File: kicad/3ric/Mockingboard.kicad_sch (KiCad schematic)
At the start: 18 parts

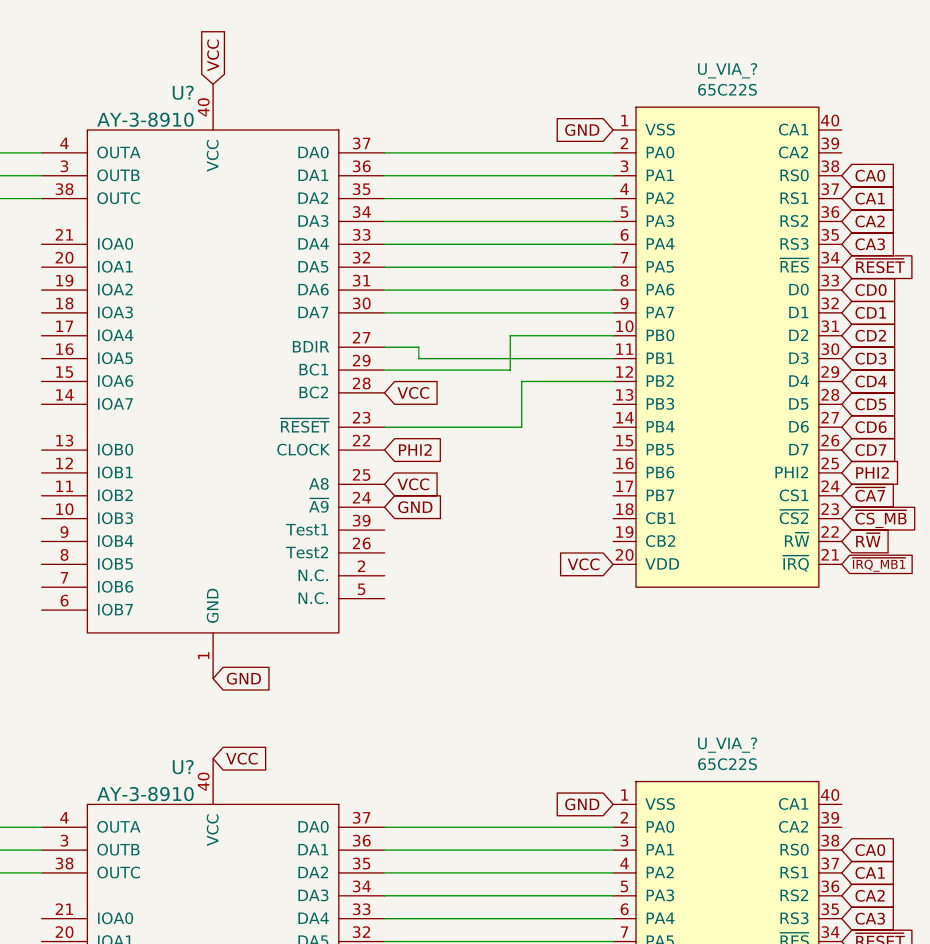
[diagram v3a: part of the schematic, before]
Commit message: update schematic based on breadboard
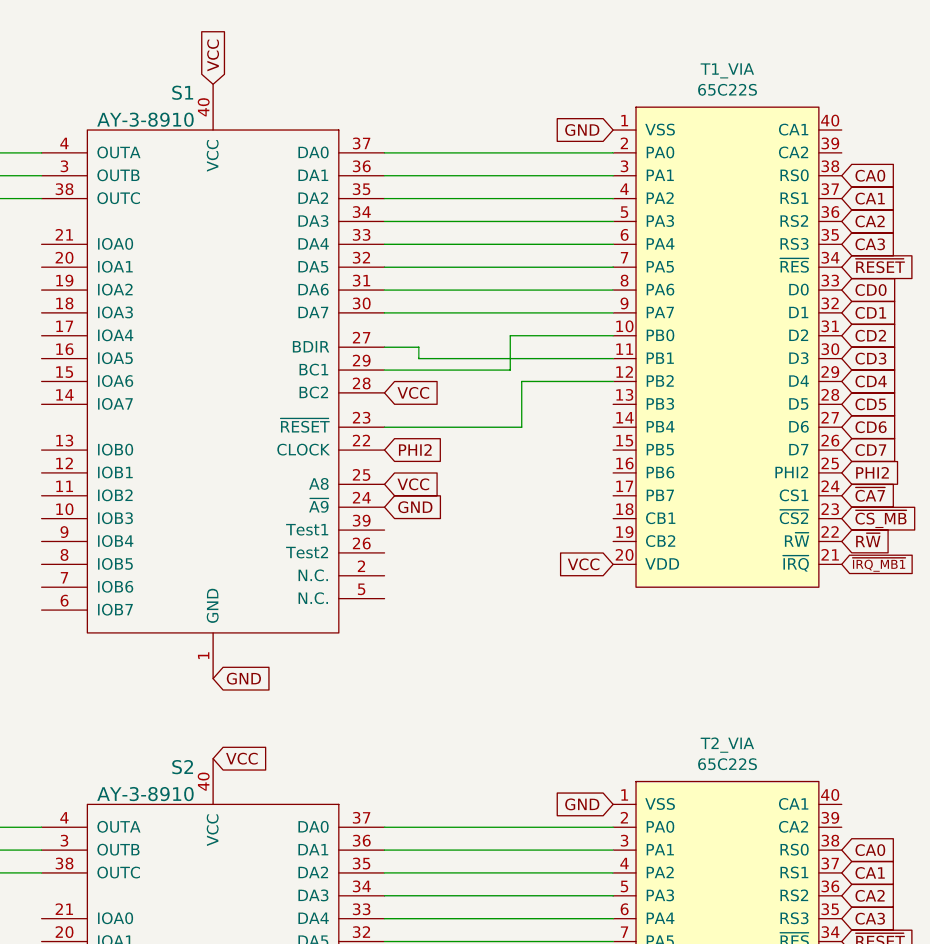
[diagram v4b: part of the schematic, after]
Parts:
- gave numbers to parts that had none: 4
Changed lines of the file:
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@@
 		(on_board yes)
 		(dnp no)
-		(property "Reference" "U_VIA_?"
+		(property "Reference" "T1_VIA"
 			(at 193.04 23.749 0)
 			(effects
@@
 			(project "3ric"
 				(path "/e63e39d7-6ac0-4ffd-8aa3-1841a4541b55/daee66e3-1acf-4bf2-888e-d1288a5b77db"
-					(reference "U_VIA_?")
+					(reference "T1_VIA")
 					(unit 1)
 				)
@@
 		(dnp no)
 		(fields_autoplaced yes)
-		(property "Reference" "U?"
+		(property "Reference" "S2"
 			(at 133.8706 101.3259 0)
 			(effects
@@
 			(project "3ric"
 				(path "/e63e39d7-6ac0-4ffd-8aa3-1841a4541b55/daee66e3-1acf-4bf2-888e-d1288a5b77db"
-					(reference "U?")
+					(reference "S2")
 					(unit 1)
 				)
@@
 		(on_board yes)
 		(dnp no)
-		(property "Reference" "U_VIA_?"
+		(property "Reference" "T2_VIA"
 			(at 193.04 98.679 0)
 			(effects
@@
 			(project "3ric"
 				(path "/e63e39d7-6ac0-4ffd-8aa3-1841a4541b55/daee66e3-1acf-4bf2-888e-d1288a5b77db"
-					(reference "U_VIA_?")
+					(reference "T2_VIA")
 					(unit 1)
 				)
@@
 		(dnp no)
 		(fields_autoplaced yes)
-		(property "Reference" "U?"
+		(property "Reference" "S1"
 			(at 133.8706 26.3959 0)
 			(effects
@@
 			(project "3ric"
 				(path "/e63e39d7-6ac0-4ffd-8aa3-1841a4541b55/daee66e3-1acf-4bf2-888e-d1288a5b77db"
-					(reference "U?")
+					(reference "S1")
 					(unit 1)
 				)

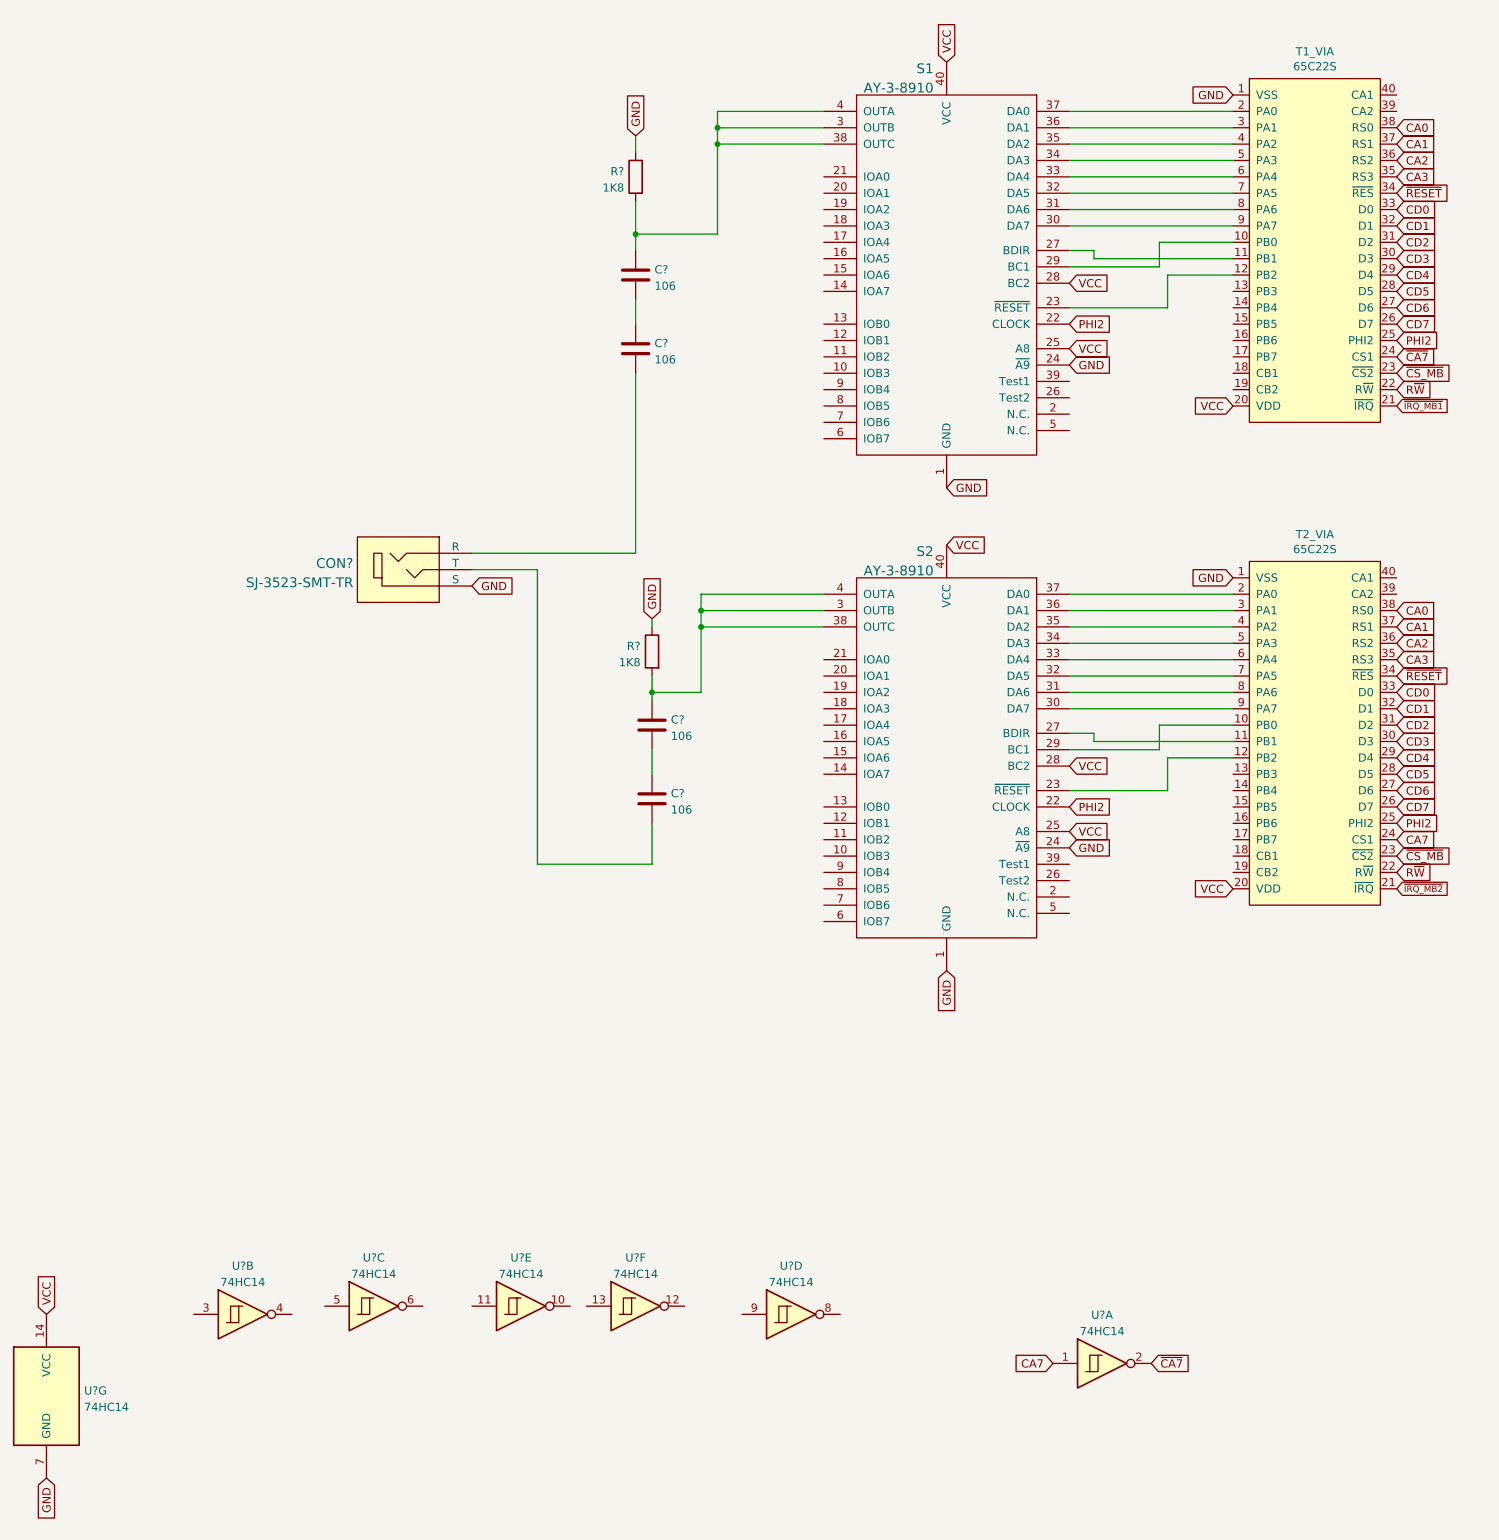
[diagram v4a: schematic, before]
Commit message: completed?  Everything wired in layout creator and first draft of completed schematic
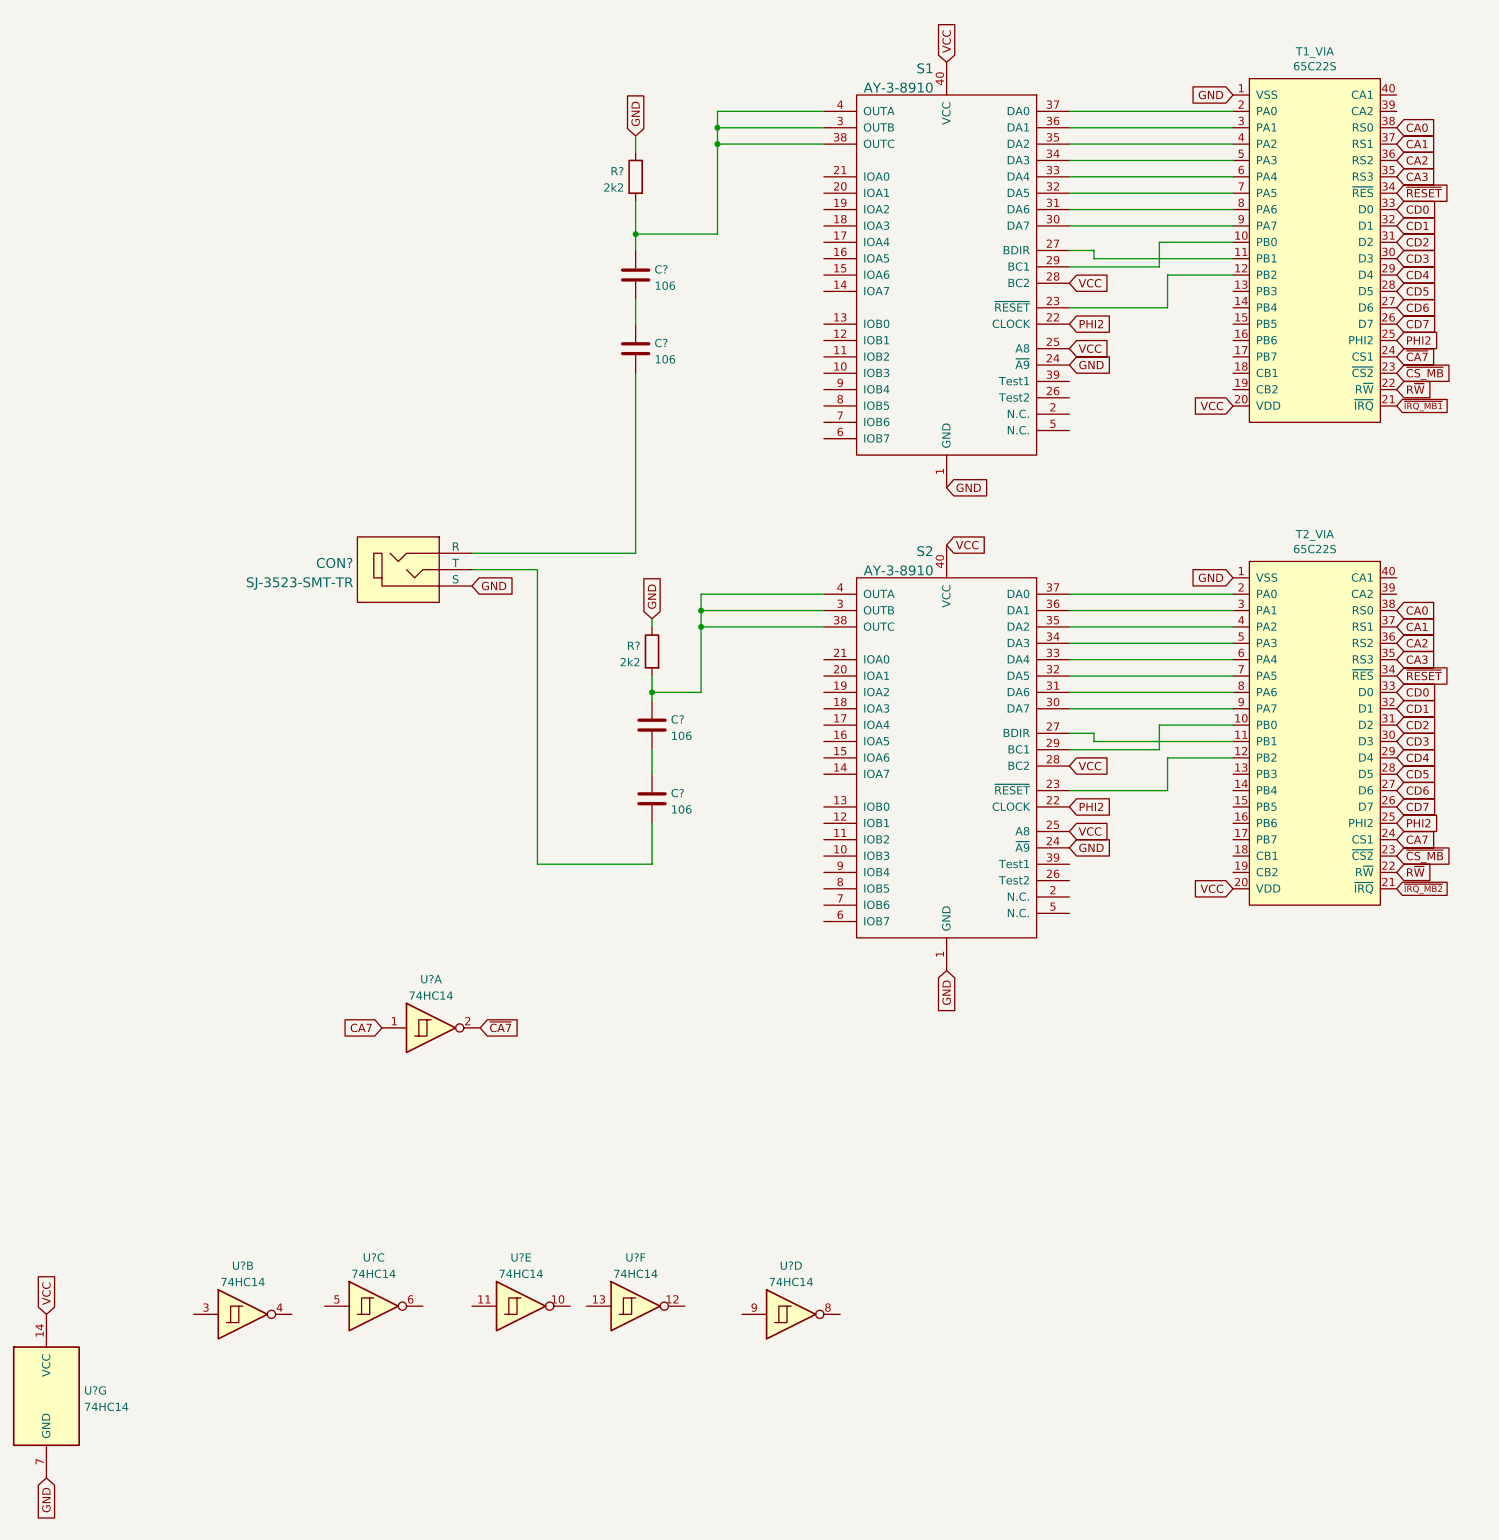
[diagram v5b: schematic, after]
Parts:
- R? (x2): value 1K8 -> 2k2
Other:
- moved on the sheet: U?A
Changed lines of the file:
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@@
 	(global_label "~{CA7}"
 		(shape input)
-		(at 167.64 227.33 0)
-		(fields_autoplaced yes)
-		(effects
-			(font
-				(size 1.27 1.27)
-			)
-			(justify left)
-		)
-		(property "Intersheetrefs" "${INTERSHEET_REFS}"
-			(at 173.6212 227.2506 0)
+		(at 63.5 175.26 0)
+		(fields_autoplaced yes)
+		(effects
+			(font
+				(size 1.27 1.27)
+			)
+			(justify left)
+		)
+		(property "Intersheetrefs" "${INTERSHEET_REFS}"
+			(at 69.4812 175.1806 0)
 			(effects
 				(font
@@
 	(global_label "CA7"
 		(shape input)
-		(at 152.4 227.33 180)
+		(at 48.26 175.26 180)
 		(fields_autoplaced yes)
 		(effects
@@
 		)
 		(property "Intersheetrefs" "${INTERSHEET_REFS}"
-			(at 146.4188 227.2506 0)
+			(at 42.2788 175.1806 0)
 			(effects
 				(font
@@
 			)
 		)
-		(property "Value" "1K8"
+		(property "Value" "2k2"
 			(at 85.852 44.8822 0)
 			(effects
@@
 	(symbol
 		(lib_id "74xx:74HC14")
-		(at 160.02 227.33 0)
+		(at 55.88 175.26 0)
 		(unit 1)
 		(exclude_from_sim no)
@@
 		(fields_autoplaced yes)
 		(property "Reference" "U?"
-			(at 160.02 219.8202 0)
+			(at 55.88 167.7502 0)
 			(effects
 				(font
@@
 		)
 		(property "Value" "74HC14"
-			(at 160.02 222.3571 0)
+			(at 55.88 170.2871 0)
 			(effects
 				(font
@@
 		)
 		(property "Footprint" ""
-			(at 160.02 227.33 0)
+			(at 55.88 175.26 0)
 			(effects
 				(font
@@
 		)
 		(property "Datasheet" "http://www.ti.com/lit/gpn/sn74HC14"
-			(at 160.02 227.33 0)
+			(at 55.88 175.26 0)
 			(effects
 				(font
@@
 		)
 		(property "Description" ""
-			(at 160.02 227.33 0)
+			(at 55.88 175.26 0)
 			(effects
 				(font
@@
 			)
 		)
-		(property "Value" "1K8"
+		(property "Value" "2k2"
 			(at 88.392 118.5422 0)
 			(effects

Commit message: cleaning up of the schematic
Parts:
- removed U? (x7): 74HC14, symbol 74xx:74HC14
- added D10, D11, D12, D7, D8, D9: D, Diode_THT:D_A-405_P10.16mm_Horizontal, symbol Device:D
- C48, C49, C50, C51: renamed from C?; footprint (none) -> Capacitor_THT:C_Axial_L3.8mm_D2.6mm_P7.50mm_Horizontal
- R37, R38: renamed from R?; footprint (none) -> Resistor_THT:R_Axial_DIN0207_L6.3mm_D2.5mm_P7.62mm_Horizontal
- S1, S2: footprint (none) -> Package_DIP:DIP-40_W15.24mm_Socket
- gave numbers to parts that had none: 1
- renumbered T1_VIA to T1_VIA1, T2_VIA to T2_VIA1
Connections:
- new net: C48.1, D7.1 (K), D8.1 (K), D9.1 (K), R37.2
- new net: D11.2 (A), S2.3 (OUTB)
- new net: D12.2 (A), S2.38 (OUTC)
- new net: D10.2 (A), S2.4 (OUTA)
- new net: C50.1, D10.1 (K), D11.1 (K), D12.1 (K), R38.2
- new net: D8.2 (A), S1.3 (OUTB)
- new net: D7.2 (A), S1.4 (OUTA)
- new net: D9.2 (A), S1.38 (OUTC)
- no-connect marks 0 -> 58
